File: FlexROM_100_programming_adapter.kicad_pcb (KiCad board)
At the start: 2 copper layers, 16.8 x 34.5 mm, 3 parts, among them J1 LH535618 Socket, U1 28C256 pinout to programmer

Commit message: minor touches
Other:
- board text added: "DIP-28x0.6" socket this side"
- board text removed: "DIP28 x 600 mil socket this side"
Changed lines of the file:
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@@
       (effects (font (size 1 1) (thickness 0.15)))
     )
+    (fp_line (start 8.382 -17.272) (end -8.382 -17.272) (layer F.CrtYd) (width 0.01))
+    (fp_line (start 8.382 17.272) (end 8.382 -17.272) (layer F.CrtYd) (width 0.01))
+    (fp_line (start -8.382 17.272) (end 8.382 17.272) (layer F.CrtYd) (width 0.01))
     (fp_line (start -8.382 -17.272) (end -8.382 17.272) (layer F.CrtYd) (width 0.01))
-    (fp_line (start -8.382 17.272) (end 8.382 17.272) (layer F.CrtYd) (width 0.01))
-    (fp_line (start 8.382 17.272) (end 8.382 -17.272) (layer F.CrtYd) (width 0.01))
-    (fp_line (start 8.382 -17.272) (end -8.382 -17.272) (layer F.CrtYd) (width 0.01))
     (fp_text user %R (at 0 0) (layer F.Fab)
       (effects (font (size 1 1) (thickness 0.15)))
@@
       (effects (font (size 1 1) (thickness 0.15)))
     )
+    (fp_line (start 8.382 -17.272) (end -8.382 -17.272) (layer F.CrtYd) (width 0.01))
+    (fp_line (start 8.382 17.272) (end 8.382 -17.272) (layer F.CrtYd) (width 0.01))
+    (fp_line (start -8.382 17.272) (end 8.382 17.272) (layer F.CrtYd) (width 0.01))
     (fp_line (start -8.382 -17.272) (end -8.382 17.272) (layer F.CrtYd) (width 0.01))
-    (fp_line (start -8.382 17.272) (end 8.382 17.272) (layer F.CrtYd) (width 0.01))
-    (fp_line (start 8.382 17.272) (end 8.382 -17.272) (layer F.CrtYd) (width 0.01))
-    (fp_line (start 8.382 -17.272) (end -8.382 -17.272) (layer F.CrtYd) (width 0.01))
     (fp_text user %R (at 0.27 3.12) (layer F.Fab)
       (effects (font (size 1 1) (thickness 0.15)))
@@
     (effects (font (size 1 1) (thickness 0.15)) (justify mirror))
   )
-  (gr_text "DIP28 x 600 mil socket this side" (at 143.523 100 -90) (layer F.SilkS)
+  (gr_text "DIP-28x0.6\" socket this side" (at 143.523 100 -90) (layer F.SilkS)
     (effects (font (size 0.8 0.8) (thickness 0.1)))
   )

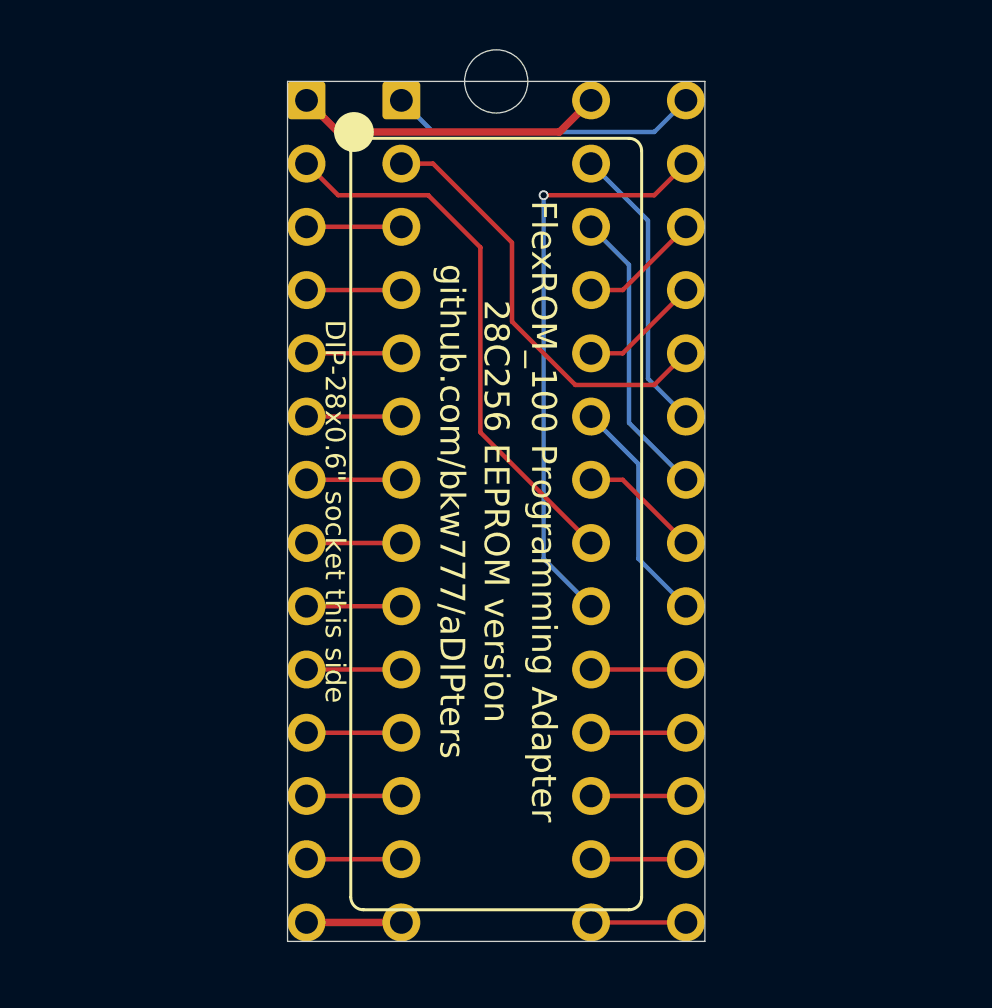
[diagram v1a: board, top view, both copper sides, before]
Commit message: add FlashROM_100_tsop
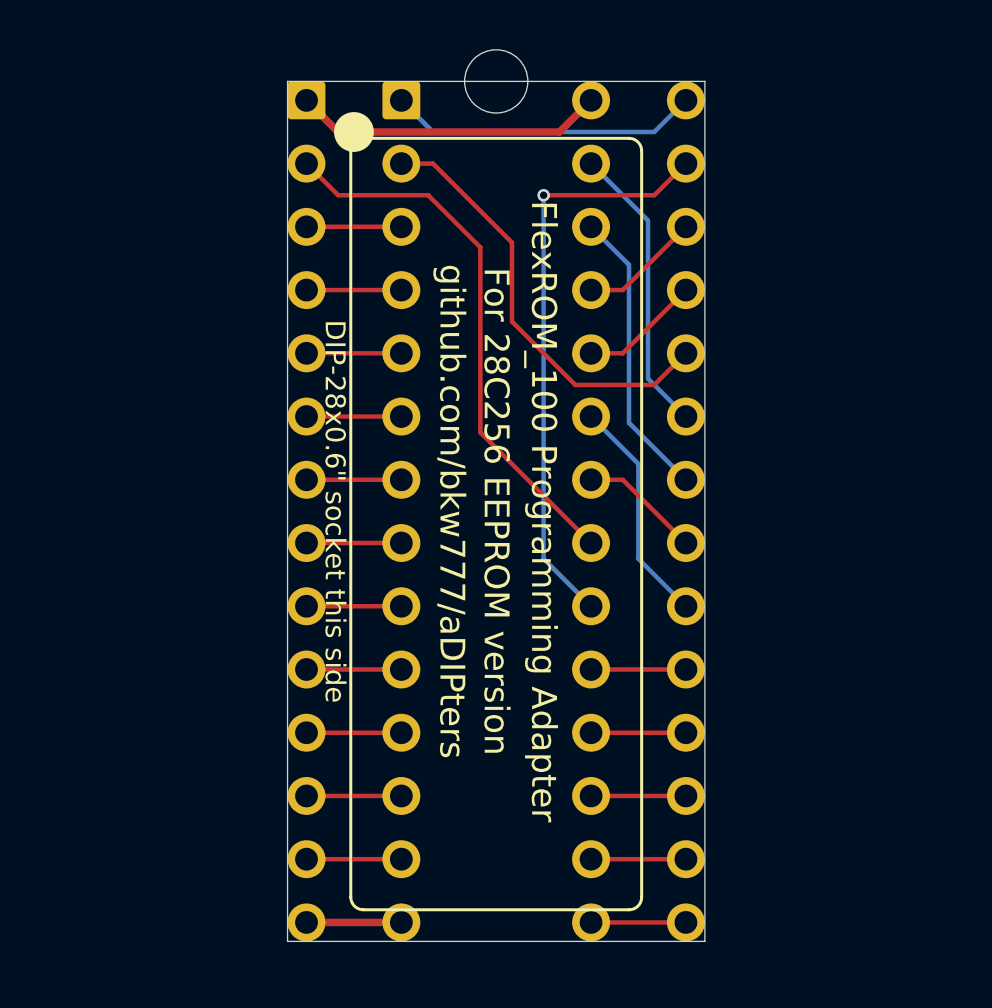
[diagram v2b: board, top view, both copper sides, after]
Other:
- net class Default: via_dia 0.4 -> 0.5; via_drill 0.25 -> 0.3
- rule via_min_drill: 0.25 -> 0.3
- rule via_min_size: 0.4 -> 0.5
- board text added: "For 28C256 EEPROM version"
- board text removed: "28C256 EEPROM version"
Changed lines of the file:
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@@
-(kicad_pcb (version 20171130) (host pcbnew 5.1.7-a382d34a8~87~ubuntu20.04.1)
+(kicad_pcb (version 20171130) (host pcbnew 5.1.9-73d0e3b20d~88~ubuntu20.10.1)
   (general
     (thickness 1.6)
@@
     (nets 29)
   )
-  (page A4)
+  (page USLetter)
+  (title_block
+    (title "Programming Adapter for FlexROM_100")
+    (date 2021-03-07)
+    (rev 002)
+    (company "Brian K. White - b.kenyon.w@gmail.com")
+  )
   (layers
     (0 F.Cu signal)
@@
     (zone_45_only no)
     (trace_min 0.16)
-    (via_size 0.4)
-    (via_drill 0.25)
-    (via_min_size 0.4)
-    (via_min_drill 0.25)
-    (uvia_size 0.4)
-    (uvia_drill 0.25)
+    (via_size 0.5)
+    (via_drill 0.3)
+    (via_min_size 0.5)
+    (via_min_drill 0.3)
+    (uvia_size 0.5)
+    (uvia_drill 0.3)
     (uvias_allowed no)
-    (uvia_min_size 0.4)
-    (uvia_min_drill 0.25)
+    (uvia_min_size 0.5)
+    (uvia_min_drill 0.3)
     (edge_width 0.05)
     (segment_width 0.2)
@@
     (pad_drill 0.9144)
     (pad_to_mask_clearance 0)
+    (solder_mask_min_width 0.22)
     (aux_axis_origin 0 0)
     (grid_origin 150 100)
     (visible_elements FFFFFF7F)
     (pcbplotparams
-      (layerselection 0x010fc_ffffffff)
+      (layerselection 0x010f0_ffffffff)
       (usegerberextensions false)
       (usegerberattributes false)
@@
       (outputformat 1)
       (mirror false)
-      (drillshape 1)
+      (drillshape 0)
       (scaleselection 1)
-      (outputdirectory ""))
+      (outputdirectory "GERBER_FlexROM_100_programming_adapter"))
   )
   (net 0 "")
@@
     (clearance 0.16)
     (trace_width 0.18)
-    (via_dia 0.4)
-    (via_drill 0.25)
-    (uvia_dia 0.4)
-    (uvia_drill 0.25)
+    (via_dia 0.5)
+    (via_drill 0.3)
+    (uvia_dia 0.5)
+    (uvia_drill 0.3)
     (add_net /A0)
     (add_net /A1)
@@
       (effects (font (size 1 1) (thickness 0.15)))
     )
+    (fp_line (start -8.382 -17.272) (end -8.382 17.272) (layer F.CrtYd) (width 0.01))
+    (fp_line (start -8.382 17.272) (end 8.382 17.272) (layer F.CrtYd) (width 0.01))
+    (fp_line (start 8.382 17.272) (end 8.382 -17.272) (layer F.CrtYd) (width 0.01))
     (fp_line (start 8.382 -17.272) (end -8.382 -17.272) (layer F.CrtYd) (width 0.01))
-    (fp_line (start 8.382 17.272) (end 8.382 -17.272) (layer F.CrtYd) (width 0.01))
-    (fp_line (start -8.382 17.272) (end 8.382 17.272) (layer F.CrtYd) (width 0.01))
-    (fp_line (start -8.382 -17.272) (end -8.382 17.272) (layer F.CrtYd) (width 0.01))
     (fp_text user %R (at 0 0) (layer F.Fab)
       (effects (font (size 1 1) (thickness 0.15)))
@@
       (effects (font (size 1 1) (thickness 0.15)))
     )
+    (fp_line (start -8.382 -17.272) (end -8.382 17.272) (layer F.CrtYd) (width 0.01))
+    (fp_line (start -8.382 17.272) (end 8.382 17.272) (layer F.CrtYd) (width 0.01))
+    (fp_line (start 8.382 17.272) (end 8.382 -17.272) (layer F.CrtYd) (width 0.01))
     (fp_line (start 8.382 -17.272) (end -8.382 -17.272) (layer F.CrtYd) (width 0.01))
-    (fp_line (start 8.382 17.272) (end 8.382 -17.272) (layer F.CrtYd) (width 0.01))
-    (fp_line (start -8.382 17.272) (end 8.382 17.272) (layer F.CrtYd) (width 0.01))
-    (fp_line (start -8.382 -17.272) (end -8.382 17.272) (layer F.CrtYd) (width 0.01))
     (fp_text user %R (at 0.27 3.12) (layer F.Fab)
       (effects (font (size 1 1) (thickness 0.15)))
@@
     )
   )
-  (gr_text "28C256 EEPROM version" (at 150 100 -90) (layer F.SilkS)
+  (gr_text "For 28C256 EEPROM version" (at 150 100 -90) (layer F.SilkS)
     (effects (font (size 1 1) (thickness 0.15)))
   )
@@
   (segment (start 157.62 96.19) (end 156.096 94.666) (width 0.18) (layer B.Cu) (net 27))
   (segment (start 151.905 87.3) (end 151.905 87.3) (width 0.18) (layer B.Cu) (net 28))
-  (via (at 151.905 87.3) (size 0.4) (drill 0.25) (layers F.Cu B.Cu) (net 28))
+  (via (at 151.905 87.3) (size 0.5) (drill 0.3) (layers F.Cu B.Cu) (net 28) (status 1000000))
   (segment (start 156.35 87.3) (end 151.905 87.3) (width 0.18) (layer F.Cu) (net 28))
   (segment (start 157.62 86.03) (end 156.35 87.3) (width 0.18) (layer F.Cu) (net 28))

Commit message: kicad 6
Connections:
- net /~CE renamed /~{CE}
- net /~OE renamed /~{OE}
- net /~WE renamed /~{WE}
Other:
- net class Default removed

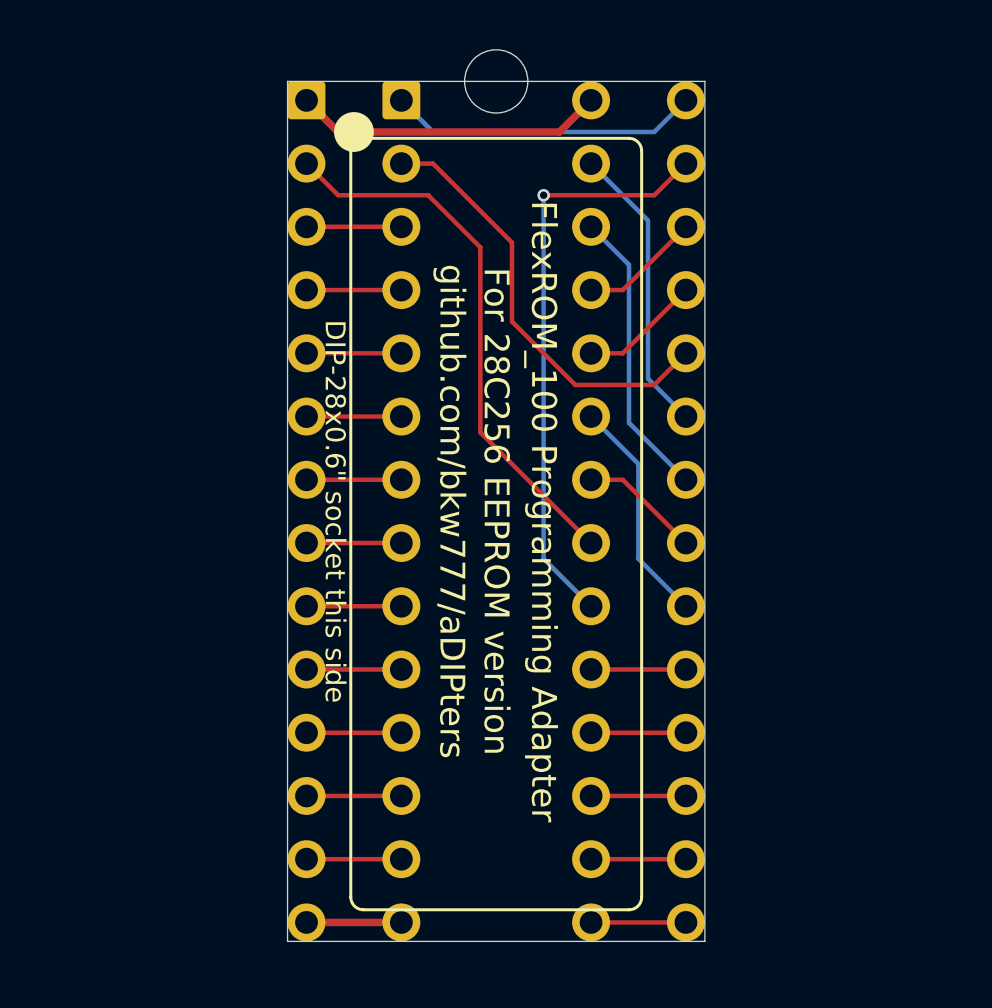
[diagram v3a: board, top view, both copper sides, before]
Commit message: programming adapter board outline & ground pour
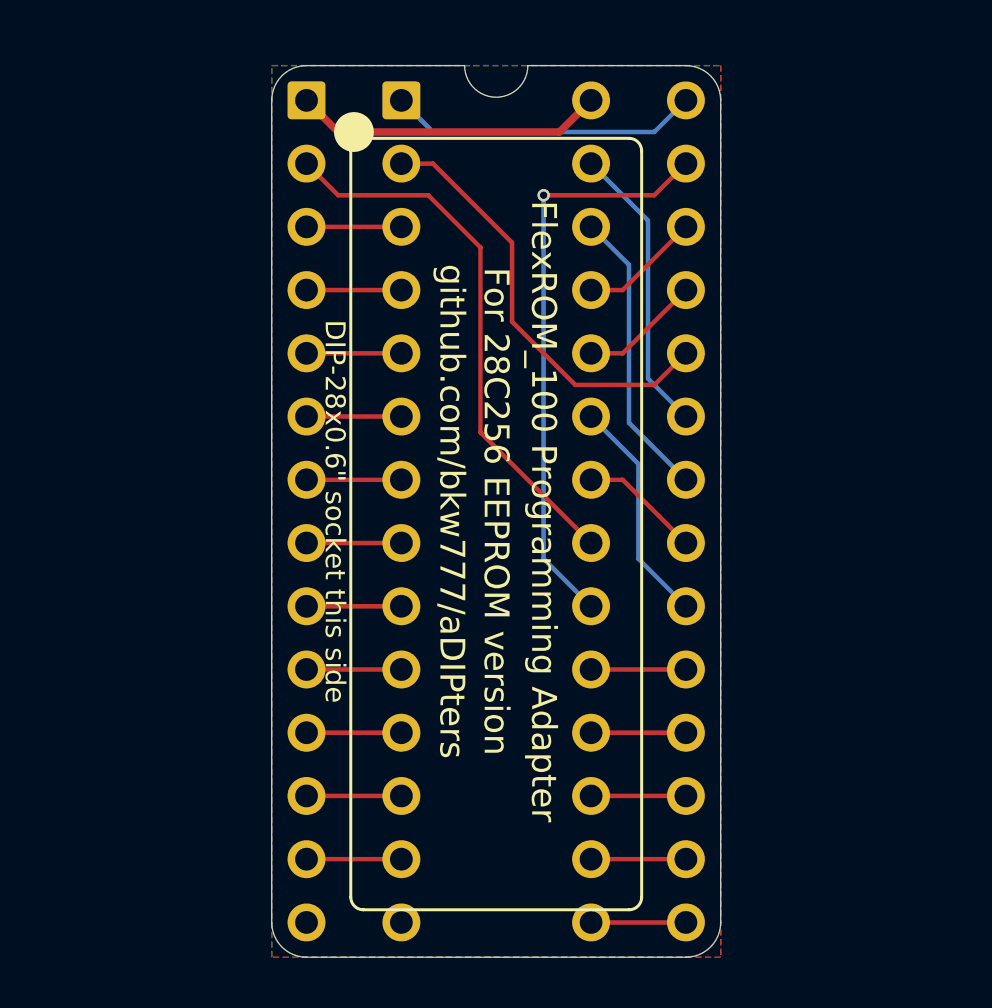
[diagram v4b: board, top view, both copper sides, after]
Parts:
- removed polarity notch: NPTH_0.1, 000_LOCAL:NPTH_0.1
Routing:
- net /GND: track 3.81 -> 0.00 mm
- added copper zone on B.Cu, net /GND
- added copper zone on F.Cu, net /GND
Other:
- board size 16.8 x 34.5 mm -> 18 x 35.8 mm
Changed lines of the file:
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@@
   (title_block
     (title "Programming Adapter for FlexROM_100")
-    (date "2021-03-07")
-    (rev "002")
+    (date "2022-10-12")
+    (rev "003")
     (company "Brian K. White - b.kenyon.w@gmail.com")
   )
@@
     )
   )
-  (footprint "000_LOCAL:NPTH_0.1" (layer "F.Cu")
-    (at 150 82.728)
-    (attr through_hole)
-    (fp_text reference "polarity notch" (at 0 2.54) (layer "F.SilkS") hide
-      (effects (font (size 1.27 1.27) (thickness 0.127)))
-    )
-    (fp_text value "NPTH_0.1" (at 0 -2.54) (layer "F.Fab")
-      (effects (font (size 1.27 1.27) (thickness 0.0127)))
-    )
-    (pad "" np_thru_hole circle locked (at 0 0) (size 2.54 2.54) (drill 2.54) (layers *.Cu *.Mask))
-  )
   (gr_line (start 152.54 82.855) (end 155.08 82.855) (layer "B.SilkS") (width 0.12))
   (gr_line (start 144.92 82.855) (end 147.46 82.855) (layer "B.SilkS") (width 0.12))
@@
   (gr_arc (start 155.842 115.494) (mid 155.69321 115.85321) (end 155.334 116.002) (layer "F.SilkS") (width 0.12))
   (gr_circle (center 144.285 84.76) (end 144.685 84.76) (layer "F.SilkS") (width 0.8) (fill none))
-  (gr_line (start 158.382 82.728) (end 158.382 117.272) (layer "Edge.Cuts") (width 0.05))
-  (gr_line (start 141.618 117.272) (end 141.618 82.728) (layer "Edge.Cuts") (width 0.05))
-  (gr_line (start 141.618 117.272) (end 158.382 117.272) (layer "Edge.Cuts") (width 0.05))
-  (gr_line (start 141.618 82.728) (end 158.382 82.728) (layer "Edge.Cuts") (width 0.05))
+  (gr_line (start 140.983 116.51) (end 140.983 83.49) (layer "Edge.Cuts") (width 0.05))
+  (gr_arc (start 159.017 116.51) (mid 158.607828 117.497828) (end 157.62 117.907) (layer "Edge.Cuts") (width 0.05))
+  (gr_line (start 157.62 117.907) (end 142.38 117.907) (layer "Edge.Cuts") (width 0.05))
+  (gr_line (start 151.27 82.093) (end 157.62 82.093) (layer "Edge.Cuts") (width 0.05))
+  (gr_arc (start 157.62 82.093) (mid 158.607828 82.502172) (end 159.017 83.49) (layer "Edge.Cuts") (width 0.05))
+  (gr_arc (start 142.38 117.907) (mid 141.392172 117.497828) (end 140.983 116.51) (layer "Edge.Cuts") (width 0.05))
+  (gr_arc (start 151.27 82.093) (mid 150 83.363) (end 148.73 82.093) (layer "Edge.Cuts") (width 0.05))
+  (gr_line (start 159.017 116.51) (end 159.017 83.49) (layer "Edge.Cuts") (width 0.05))
+  (gr_arc (start 140.983 83.49) (mid 141.392172 82.502172) (end 142.38 82.093) (layer "Edge.Cuts") (width 0.05))
+  (gr_line (start 142.38 82.093) (end 148.73 82.093) (layer "Edge.Cuts") (width 0.05))
   (gr_text "tandy.wiki/FlexROM_100" (at 151.524 100 90) (layer "B.SilkS")
     (effects (font (size 1 1) (thickness 0.15)) (justify mirror))
@@
   (segment (start 153.81 91.11) (end 155.08 91.11) (width 0.18) (layer "F.Cu") (net 23))
   (segment (start 142.38 113.97) (end 146.19 113.97) (width 0.18) (layer "F.Cu") (net 24))
-  (segment (start 142.38 116.51) (end 146.19 116.51) (width 0.3) (layer "F.Cu") (net 25))
   (segment (start 147.46 84.76) (end 156.35 84.76) (width 0.18) (layer "B.Cu") (net 26))
   (segment (start 156.35 84.76) (end 157.62 83.49) (width 0.18) (layer "B.Cu") (net 26))
@@
   (segment (start 153.81 103.81) (end 151.905 101.905) (width 0.18) (layer "B.Cu") (net 28))
   (segment (start 151.905 101.905) (end 151.905 87.3) (width 0.18) (layer "B.Cu") (net 28))
+  (zone (net 25) (net_name "/GND") (layer "F.Cu") (hatch edge 0.508)
+    (connect_pads yes (clearance 0.2))
+    (min_thickness 0.2) (filled_areas_thickness no)
+    (fill yes (thermal_gap 0.508) (thermal_bridge_width 0.508))
+    (polygon
+      (pts
+        (xy 159.017 117.907)
+        (xy 140.983 117.907)
+        (xy 140.983 82.093)
+        (xy 159.017 82.093)
+      )
+    )
+  )
+  (zone (net 25) (net_name "/GND") (layer "B.Cu") (hatch edge 0.508)
+    (connect_pads yes (clearance 0.2))
+    (min_thickness 0.2) (filled_areas_thickness no)
+    (fill yes (thermal_gap 0.508) (thermal_bridge_width 0.508))
+    (polygon
+      (pts
+        (xy 159.017 117.907)
+        (xy 140.983 117.907)
+        (xy 140.983 82.093)
+        (xy 159.017 82.093)
+      )
+    )
+  )
 )

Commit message: various minor cleanups
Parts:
- turned J1 to 90 degrees
- turned U1 to 90 degrees
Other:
- board size 18 x 35.8 mm -> 35.8 x 18 mm
